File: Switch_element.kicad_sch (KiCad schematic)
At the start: 10 parts, among them U601 AP22653AW6-7, U602 AP22653AW6-7

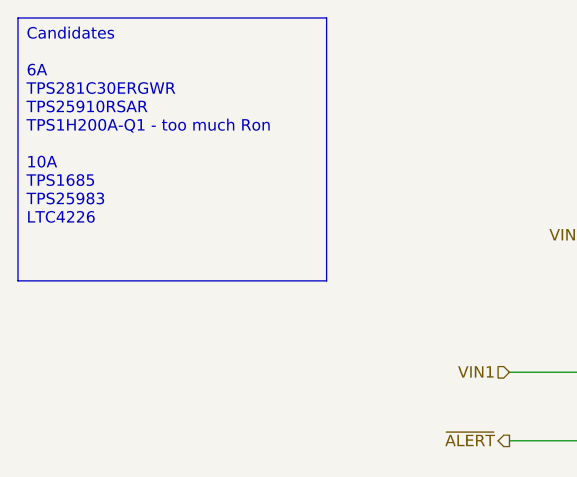
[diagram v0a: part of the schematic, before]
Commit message: replaced individual CC sourses for SOL with a single one
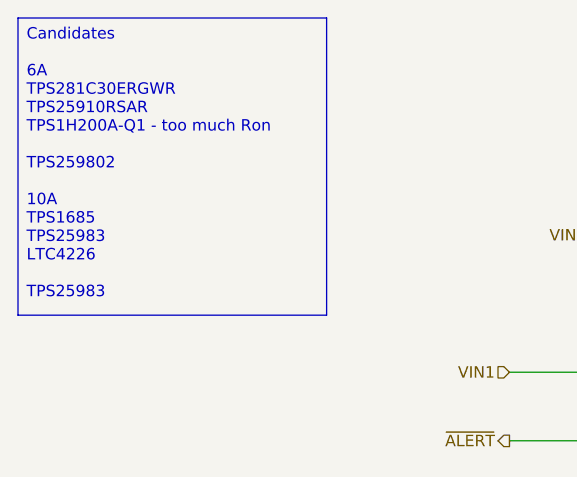
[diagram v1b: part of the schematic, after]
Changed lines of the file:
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@@
 		)
 	)
-	(text_box "Candidates\n\n6A\nTPS281C30ERGWR\nTPS25910RSAR\nTPS1H200A-Q1 - too much Ron\n\n10A\nTPS1685\nTPS25983\nLTC4226"
+	(text_box "Candidates\n\n6A\nTPS281C30ERGWR\nTPS25910RSAR\nTPS1H200A-Q1 - too much Ron\n\nTPS259802\n\n10A\nTPS1685\nTPS25983\nLTC4226\n\nTPS25983"
 		(exclude_from_sim no)
 		(at 44.45 39.37 0)
-		(size 34.29 29.21)
+		(size 34.29 33.02)
 		(margins 0.9525 0.9525 0.9525 0.9525)
 		(stroke

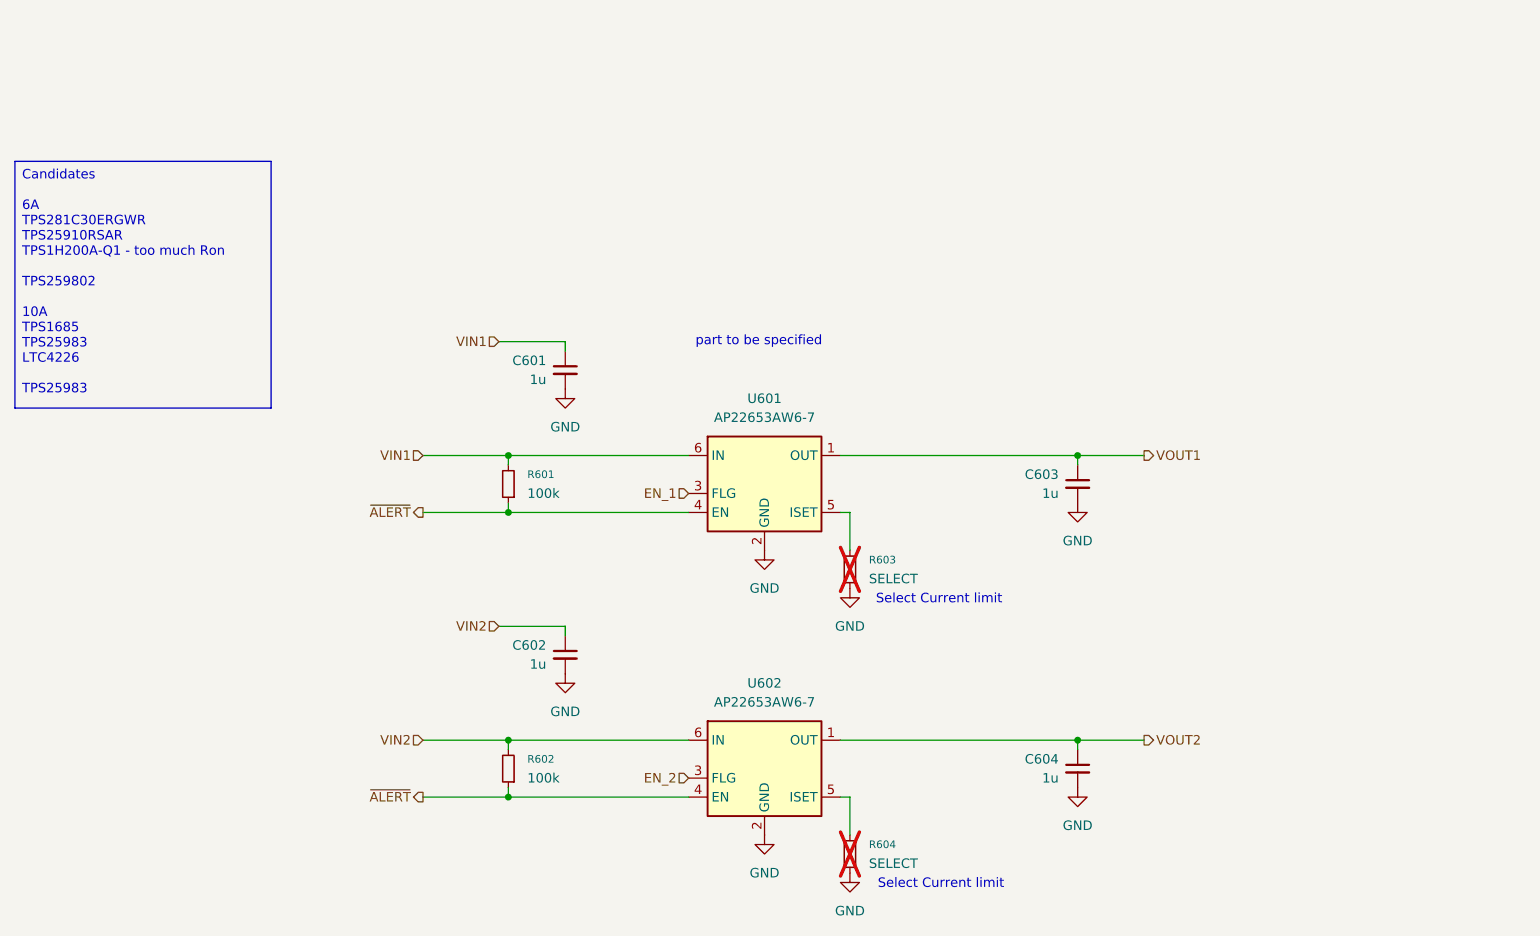
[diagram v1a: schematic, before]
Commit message: restructurization of the entire project improved
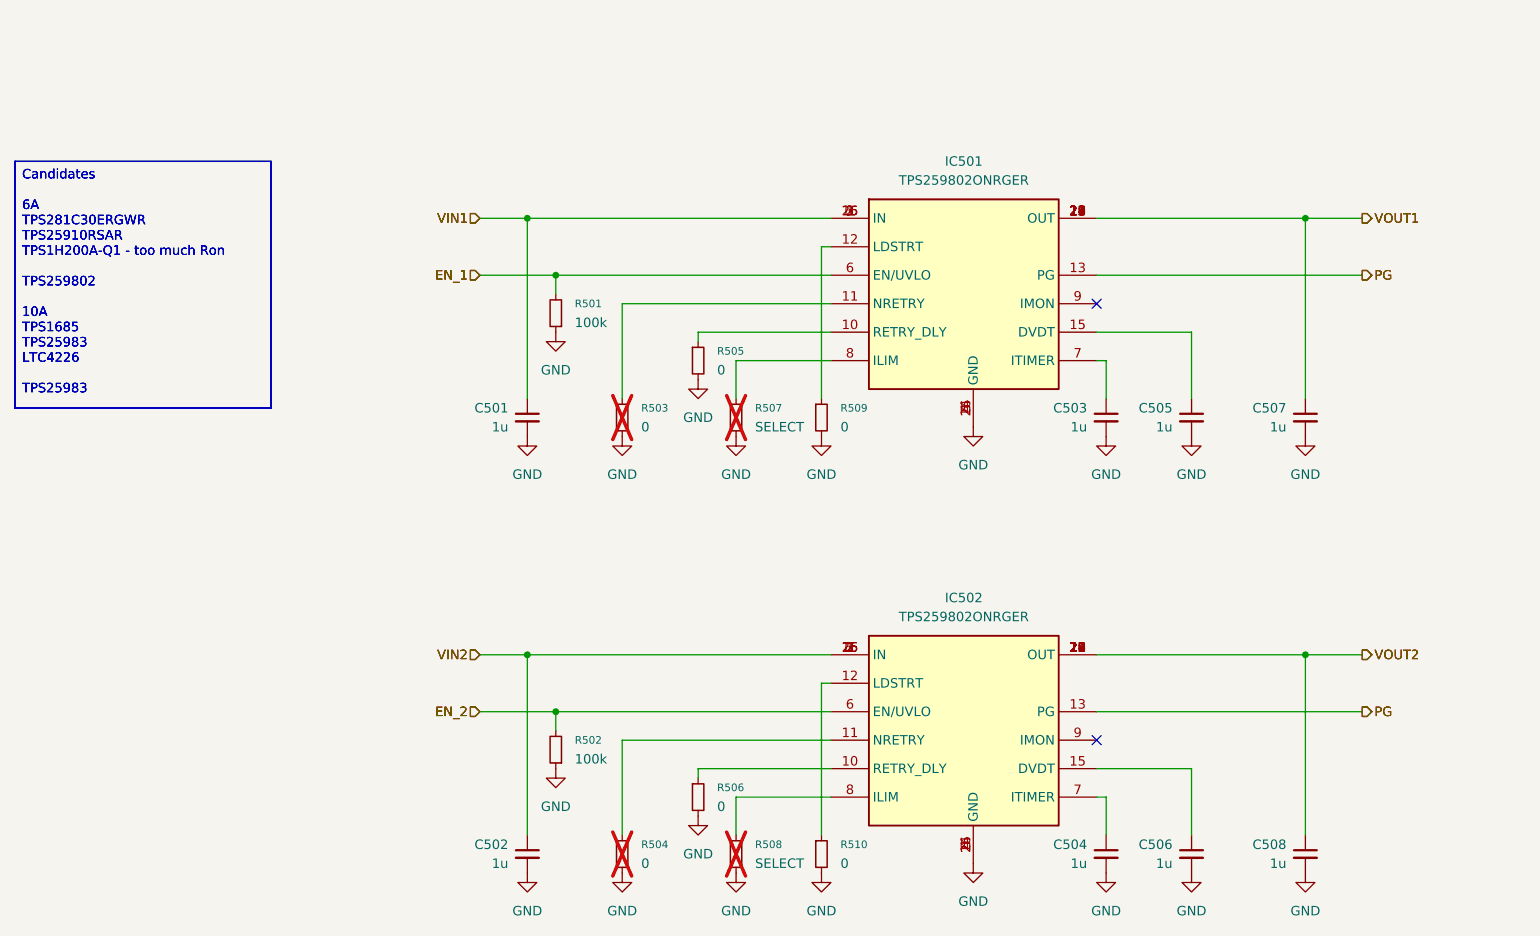
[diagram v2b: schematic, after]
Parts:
- removed C601, C602, C603, C604: 1u, Capacitor_SMD:C_0603_1608Metric_Pad1.08x0.95mm_HandSolder, symbol Device:C_Small
- removed R601, R602: 100k, Resistor_SMD:R_0603_1608Metric_Pad0.98x0.95mm_HandSolder, symbol Device:R_Small
- removed R603, R604: SELECT, Resistor_SMD:R_0603_1608Metric_Pad0.98x0.95mm_HandSolder, symbol Device:R_Small
- removed U601, U602: AP22653AW6-7, Package_TO_SOT_SMD:SOT-23-6, symbol Regulator_Linear:AP22615AWU
- added C501, C502, C503, C504, C505, C506, C507, C508: 1u, Capacitor_SMD:C_0603_1608Metric_Pad1.08x0.95mm_HandSolder, symbol Device:C_Small
- added IC501, IC502: TPS259802ONRGER, Outlines:TPS259802ONRGER, symbol TPS259802ONRGER:TPS259802ONRGER
- added R501, R502: 100k, Resistor_SMD:R_0603_1608Metric_Pad0.98x0.95mm_HandSolder, symbol Device:R_Small
- added R503, R504, R505, R506, R509, R510: 0, Resistor_SMD:R_0603_1608Metric_Pad0.98x0.95mm_HandSolder, symbol Device:R_Small
- added R507, R508: SELECT, Resistor_SMD:R_0603_1608Metric_Pad0.98x0.95mm_HandSolder, symbol Device:R_Small
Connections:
- net EN_1: now also IC501.6 (EN/UVLO), R501.2
- net EN_2: now also IC502.6 (EN/UVLO), R502.2
- net GND: now also C501.2, C502.2, C503.2, C504.2, C505.2, C506.2, C507.2, C508.2, IC501.14 (GND), IC501.26 (GND), IC501.4 (GND), IC501.5 (GND), IC502.14 (GND), IC502.26 (GND), IC502.4 (GND), IC502.5 (GND), R501.1, R502.1, R503.2, R504.2, R505.2, R506.2, R507.2, R508.2, R509.2, R510.2
- net VIN1: now also C501.1, IC501.1 (IN), IC501.16 (IN), IC501.2 (IN), IC501.25 (IN), IC501.3 (IN)
- net VIN2: now also C502.1, IC502.1 (IN), IC502.16 (IN), IC502.2 (IN), IC502.25 (IN), IC502.3 (IN)
- net VOUT1: now also C507.1, IC501.17 (OUT), IC501.18 (OUT), IC501.19 (OUT), IC501.20 (OUT), IC501.21 (OUT), IC501.22 (OUT), IC501.23 (OUT), IC501.24 (OUT)
- net VOUT2: now also C508.1, IC502.17 (OUT), IC502.18 (OUT), IC502.19 (OUT), IC502.20 (OUT), IC502.21 (OUT), IC502.22 (OUT), IC502.23 (OUT), IC502.24 (OUT)
- new net: IC502.11 (NRETRY), R504.1
- new net: IC502.8 (ILIM), R508.1
- new net: IC501.8 (ILIM), R507.1
- new net: IC502.12 (LDSTRT), R510.1
- new net: IC501.10 (RETRY_DLY), R505.1
- new net: C506.1, IC502.15 (DVDT)
- new net: IC501.11 (NRETRY), R503.1
- new net: IC501.12 (LDSTRT), R509.1
- new net: C505.1, IC501.15 (DVDT)
- new net: C503.1, IC501.7 (ITIMER)
- new net: IC502.10 (RETRY_DLY), R506.1
- new net: C504.1, IC502.7 (ITIMER)
- new net PG: IC501.13 (PG), IC502.13 (PG)
- no-connect marks 0 -> 2
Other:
- note removed: "Select Current limit"
- note removed: "part to be specified"

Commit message: added universal switch, added simples current source, reworked test schematic and pcb
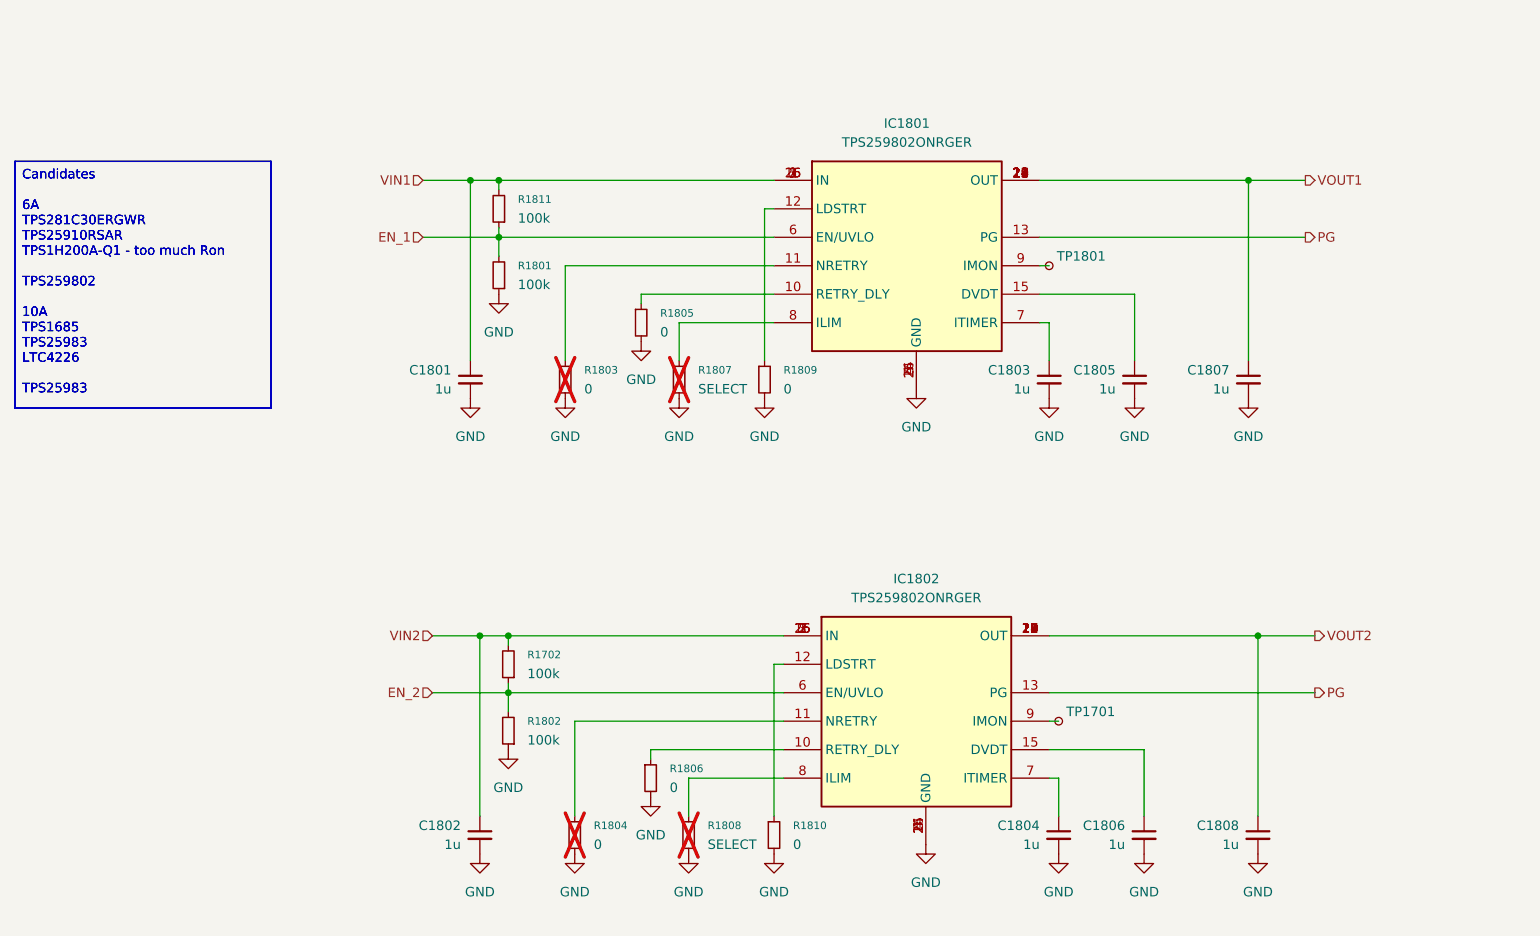
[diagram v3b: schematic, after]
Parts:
- removed C501, C502, C503, C504, C505, C506, C507, C508: 1u, Capacitor_SMD:C_0603_1608Metric_Pad1.08x0.95mm_HandSolder, symbol Device:C_Small
- removed IC501, IC502: TPS259802ONRGER, Outlines:TPS259802ONRGER, symbol TPS259802ONRGER:TPS259802ONRGER
- removed R501, R502: 100k, Resistor_SMD:R_0603_1608Metric_Pad0.98x0.95mm_HandSolder, symbol Device:R_Small
- removed R503, R504, R505, R506, R509, R510: 0, Resistor_SMD:R_0603_1608Metric_Pad0.98x0.95mm_HandSolder, symbol Device:R_Small
- removed R507, R508: SELECT, Resistor_SMD:R_0603_1608Metric_Pad0.98x0.95mm_HandSolder, symbol Device:R_Small
- added C1801, C1802, C1803, C1804, C1805, C1806, C1807, C1808: 1u, Capacitor_SMD:C_0603_1608Metric_Pad1.08x0.95mm_HandSolder, symbol Device:C_Small
- added IC1801, IC1802: TPS259802ONRGER, Outlines:TPS259802ONRGER, symbol TPS259802ONRGER:TPS259802ONRGER
- added R1702, R1801, R1802, R1811: 100k, Resistor_SMD:R_0603_1608Metric_Pad0.98x0.95mm_HandSolder, symbol Device:R_Small
- added R1803, R1804, R1805, R1806, R1809, R1810: 0, Resistor_SMD:R_0603_1608Metric_Pad0.98x0.95mm_HandSolder, symbol Device:R_Small
- added R1807, R1808: SELECT, Resistor_SMD:R_0603_1608Metric_Pad0.98x0.95mm_HandSolder, symbol Device:R_Small
- added TP1701, TP1801: ~, TestPoint:TestPoint_Pad_1.0x1.0mm, symbol Connector:TestPoint_Small
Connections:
- net EN_1: now also IC1801.6 (EN/UVLO), R1801.2, R1811.1
- net EN_2: now also IC1802.6 (EN/UVLO), R1702.1, R1802.2
- net GND: now also C1801.2, C1802.2, C1803.2, C1804.2, C1805.2, C1806.2, C1807.2, C1808.2, IC1801.14 (GND), IC1801.26 (GND), IC1801.4 (GND), IC1801.5 (GND), IC1802.14 (GND), IC1802.26 (GND), IC1802.4 (GND), IC1802.5 (GND), R1801.1, R1802.1, R1803.2, R1804.2, R1805.2, R1806.2, R1807.2, R1808.2, R1809.2, R1810.2
- net PG: now also IC1801.13 (PG), IC1802.13 (PG)
- net VIN1: now also C1801.1, IC1801.1 (IN), IC1801.16 (IN), IC1801.2 (IN), IC1801.25 (IN), IC1801.3 (IN), R1811.2
- net VIN2: now also C1802.1, IC1802.1 (IN), IC1802.16 (IN), IC1802.2 (IN), IC1802.25 (IN), IC1802.3 (IN), R1702.2
- net VOUT1: now also C1807.1, IC1801.17 (OUT), IC1801.18 (OUT), IC1801.19 (OUT), IC1801.20 (OUT), IC1801.21 (OUT), IC1801.22 (OUT), IC1801.23 (OUT), IC1801.24 (OUT)
- net VOUT2: now also C1808.1, IC1802.17 (OUT), IC1802.18 (OUT), IC1802.19 (OUT), IC1802.20 (OUT), IC1802.21 (OUT), IC1802.22 (OUT), IC1802.23 (OUT), IC1802.24 (OUT)
- new net: C1803.1, IC1801.7 (ITIMER)
- new net: IC1801.9 (IMON), TP1801.1
- new net: IC1802.10 (RETRY_DLY), R1806.1
- new net: IC1802.11 (NRETRY), R1804.1
- new net: IC1802.12 (LDSTRT), R1810.1
- new net: C1806.1, IC1802.15 (DVDT)
- new net: C1804.1, IC1802.7 (ITIMER)
- new net: IC1802.8 (ILIM), R1808.1
- new net: IC1802.9 (IMON), TP1701.1
- new net: C1805.1, IC1801.15 (DVDT)
- new net: IC1801.12 (LDSTRT), R1809.1
- new net: IC1801.11 (NRETRY), R1803.1
- new net: IC1801.8 (ILIM), R1807.1
- new net: IC1801.10 (RETRY_DLY), R1805.1
- no-connect marks 2 -> 0

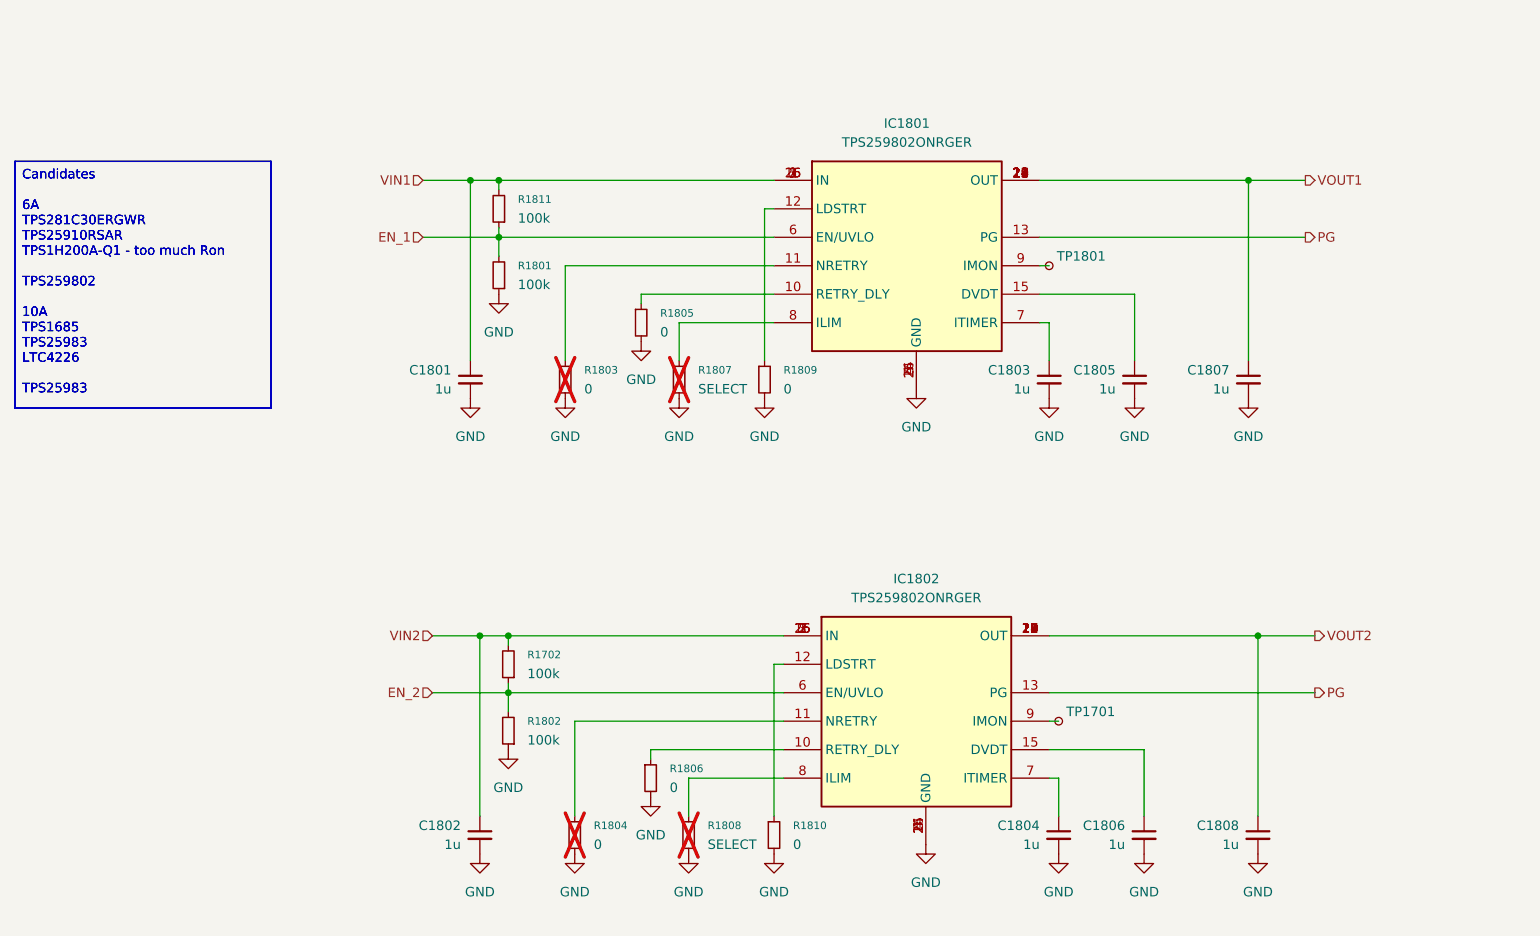
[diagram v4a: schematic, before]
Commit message: changes based on test board manufacturing, mostly added voltage dividers
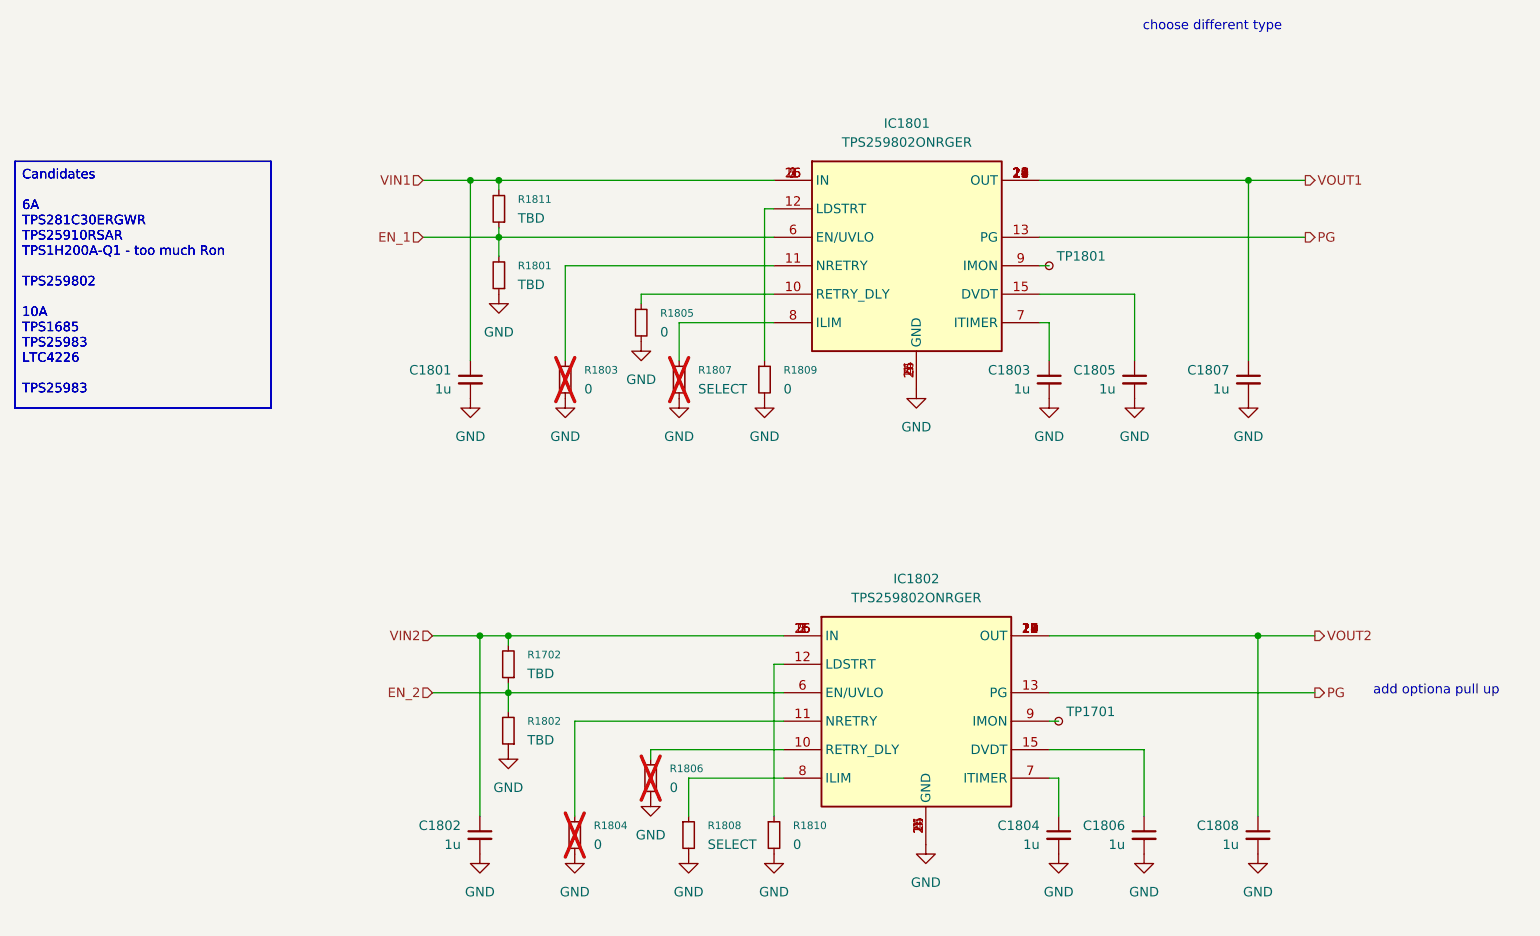
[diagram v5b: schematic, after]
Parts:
- R1702, R1801, R1802, R1811: value 100k -> TBD
- R1806: now not fitted
- R1808: now fitted
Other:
- note added: "add optiona pull up"
- note added: "choose different type"

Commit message: progress on CORE pcb
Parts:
- renumbered C1801 to C301, C1803 to C302, C1805 to C303, C1807 to C304, C1802 to C305, C1804 to C306, C1806 to C307, C1808 to C308, IC1801 to IC301, IC1802 to IC302, R1811 to R301, R1801 to R302, R1805 to R303, R1803 to R304, R1807 to R305, R1809 to R306, R1702 to R307, R1802 to R308, R1806 to R309, R1804 to R310, R1808 to R311, R1810 to R312, TP1801 to TP301, TP1701 to TP302
